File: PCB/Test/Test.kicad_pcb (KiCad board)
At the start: 2 copper layers, 50 x 50 mm, 16 parts, among them J1 USB-C, J2 USB-C, J3 USB-C, J4 USB-C, J5 USB-C, J6 USB-C, J7 USB-C, J8 USB-C, U1 ESP32-PICO-MINI-02, U2 ESP32-PICO-MINI-02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

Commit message: rotate direction
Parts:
- added J9: Conn_01x04, RevK:JLC-PinHeader_1x04_P2.54mm_Right, F.Cu at (104.0, 98.0)
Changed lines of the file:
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@@
   (net 327 "unconnected-(J8-PadB8)")
   (net 328 "unconnected-(J8-PadS1)")
+  (net 329 "unconnected-(J9-Pad1)")
+  (net 330 "unconnected-(J9-Pad2)")
+  (net 331 "unconnected-(J9-Pad3)")
+  (net 332 "unconnected-(J9-Pad4)")
   (footprint "RevK:ESP32-PICO-MINI-02" (layer "F.Cu")
     (at 65 75 90)
@@
     )
   )
+  (footprint "RevK:JLC-PinHeader_1x04_P2.54mm_Right" (layer "F.Cu")
+    (at 104 98)
+    (descr "Through hole angled pin header, 1x04, 2.54mm pitch, 6mm pin length, single row")
+    (tags "Through hole angled pin header THT 1x04 2.54mm single row")
+    (property "Sheetfile" "Test.kicad_sch")
+    (property "Sheetname" "")
+    (attr through_hole)
+    (fp_text reference "J9" (at 4.385 -2.27) (layer "F.SilkS") hide
+      (effects (font (size 1 1) (thickness 0.15)))
+    )
+    (fp_text value "Conn_01x04" (at -6.08 0.655 270) (layer "F.Fab") hide
+      (effects (font (size 1 1) (thickness 0.15)))
+    )
+    (fp_text user "${REFERENCE}" (at 0 2.77) (layer "F.Fab")
+      (effects (font (size 1 1) (thickness 0.15)))
+    )
+    (fp_line (start -5.08 1.27) (end -5.08 -1.27) (layer "F.CrtYd") (width 0.12))
+    (fp_line (start -5.08 -1.27) (end 5.08 -1.27) (layer "F.CrtYd") (width 0.12))
+    (fp_line (start 5.08 1.27) (end -5.08 1.27) (layer "F.CrtYd") (width 0.12))
+    (fp_line (start 5.08 -1.27) (end 5.08 1.27) (layer "F.CrtYd") (width 0.12))
+    (fp_line (start 0.95 -0.32) (end 0.95 1.5) (layer "F.Fab") (width 0.1))
+    (fp_line (start 4.445 1.5) (end 5.08 2.135) (layer "F.Fab") (width 0.1))
+    (fp_line (start -3.49 -0.32) (end -4.13 -0.32) (layer "F.Fab") (width 0.1))
+    (fp_line (start -4.13 4.04) (end -4.13 10.04) (layer "F.Fab") (width 0.1))
+    (fp_line (start -0.95 4.04) (end -0.95 10.04) (layer "F.Fab") (width 0.1))
+    (fp_line (start 5.08 4.04) (end -5.08 4.04) (layer "F.Fab") (width 0.1))
+    (fp_line (start -0.95 -0.32) (end -0.95 1.5) (layer "F.Fab") (width 0.1))
+    (fp_line (start 3.49 4.04) (end 3.49 10.04) (layer "F.Fab") (width 0.1))
+    (fp_line (start 0.95 4.04) (end 0.95 10.04) (layer "F.Fab") (width 0.1))
+    (fp_line (start -0.95 10.04) (end -1.59 10.04) (layer "F.Fab") (width 0.1))
+    (fp_line (start 1.59 -0.32) (end 0.95 -0.32) (layer "F.Fab") (width 0.1))
+    (fp_line (start -3.49 4.04) (end -3.49 10.04) (layer "F.Fab") (width 0.1))
+    (fp_line (start -3.49 -0.32) (end -3.49 1.5) (layer "F.Fab") (width 0.1))
+    (fp_line (start -1.59 -0.32) (end -1.59 1.5) (layer "F.Fab") (width 0.1))
+    (fp_line (start -5.08 4.04) (end -5.08 1.5) (layer "F.Fab") (width 0.1))
+    (fp_line (start 1.59 10.04) (end 0.95 10.04) (layer "F.Fab") (width 0.1))
+    (fp_line (start 4.13 4.04) (end 4.13 10.04) (layer "F.Fab") (width 0.1))
+    (fp_line (start 5.08 2.135) (end 5.08 4.04) (layer "F.Fab") (width 0.1))
+    (fp_line (start 1.59 4.04) (end 1.59 10.04) (layer "F.Fab") (width 0.1))
+    (fp_line (start 4.13 -0.32) (end 3.49 -0.32) (layer "F.Fab") (width 0.1))
+    (fp_line (start -1.59 4.04) (end -1.59 10.04) (layer "F.Fab") (width 0.1))
+    (fp_line (start 3.49 -0.32) (end 3.49 1.5) (layer "F.Fab") (width 0.1))
+    (fp_line (start 4.13 10.04) (end 3.49 10.04) (layer "F.Fab") (width 0.1))
+    (fp_line (start -4.13 -0.32) (end -4.13 1.5) (layer "F.Fab") (width 0.1))
+    (fp_line (start 1.59 -0.32) (end 1.59 1.5) (layer "F.Fab") (width 0.1))
+    (fp_line (start 4.13 -0.32) (end 4.13 1.5) (layer "F.Fab") (width 0.1))
+    (fp_line (start -3.49 10.04) (end -4.13 10.04) (layer "F.Fab") (width 0.1))
+    (fp_line (start -5.08 1.5) (end 4.445 1.5) (layer "F.Fab") (width 0.1))
+    (fp_line (start -0.95 -0.32) (end -1.59 -0.32) (layer "F.Fab") (width 0.1))
+    (pad "1" thru_hole rect (at -3.81 0 270) (size 1.7 1.7) (drill 1) (layers *.Cu *.Mask)
+      (net 329 "unconnected-(J9-Pad1)") (pinfunction "Pin_1") (pintype "passive"))
+    (pad "2" thru_hole oval (at -1.27 0 270) (size 1.7 1.7) (drill 1) (layers *.Cu *.Mask)
+      (net 330 "unconnected-(J9-Pad2)") (pinfunction "Pin_2") (pintype "passive"))
+    (pad "3" thru_hole oval (at 1.27 0 270) (size 1.7 1.7) (drill 1) (layers *.Cu *.Mask)
+      (net 331 "unconnected-(J9-Pad3)") (pinfunction "Pin_3") (pintype "passive"))
+    (pad "4" thru_hole circle (at 3.81 0 270) (size 1.7 1.7) (drill 1) (layers *.Cu *.Mask)
+      (net 332 "unconnected-(J9-Pad4)") (pinfunction "Pin_4") (pintype "passive"))
+    (model "${KICAD6_3DMODEL_DIR}/Connector_PinHeader_2.54mm.3dshapes/PinHeader_1x04_P2.54mm_Horizontal.wrl"
+      (offset (xyz 3.81 0 0))
+      (scale (xyz 1 1 1))
+      (rotate (xyz 0 0 90))
+    )
+  )

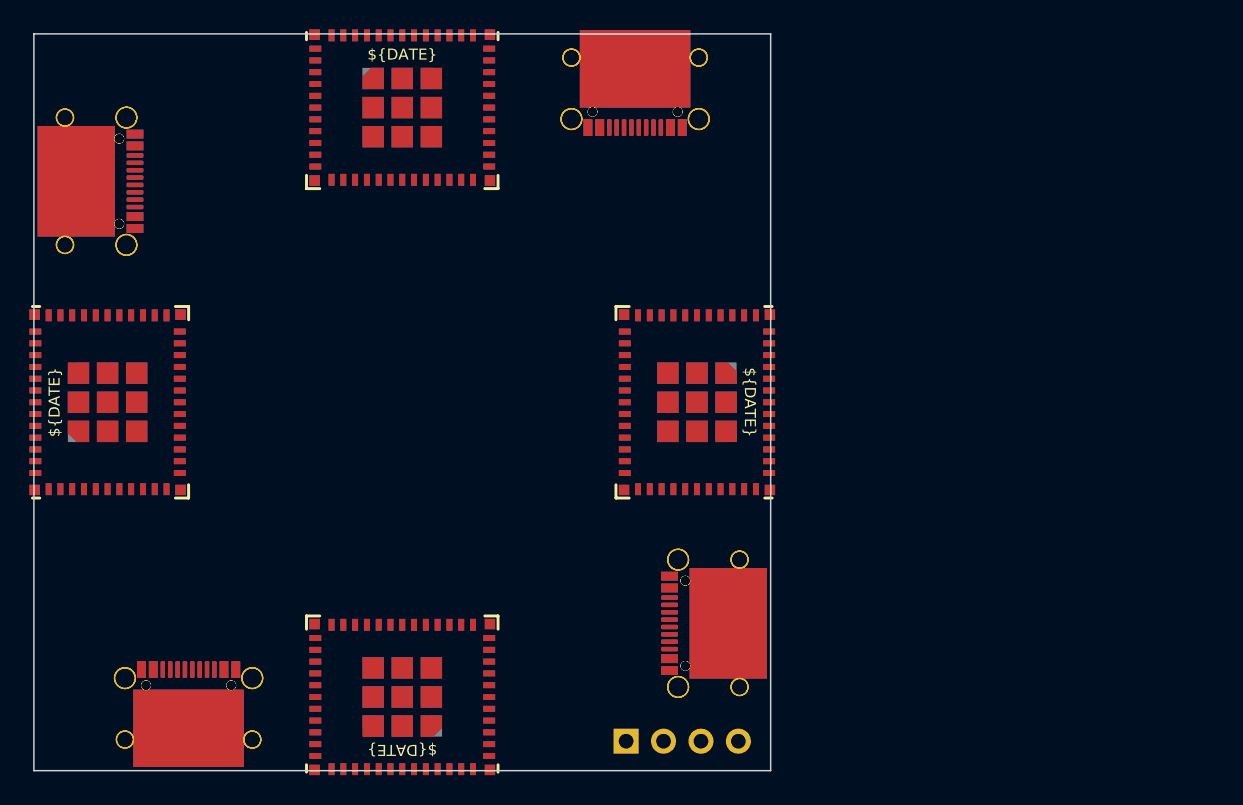
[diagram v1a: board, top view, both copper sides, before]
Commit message: Updated test case
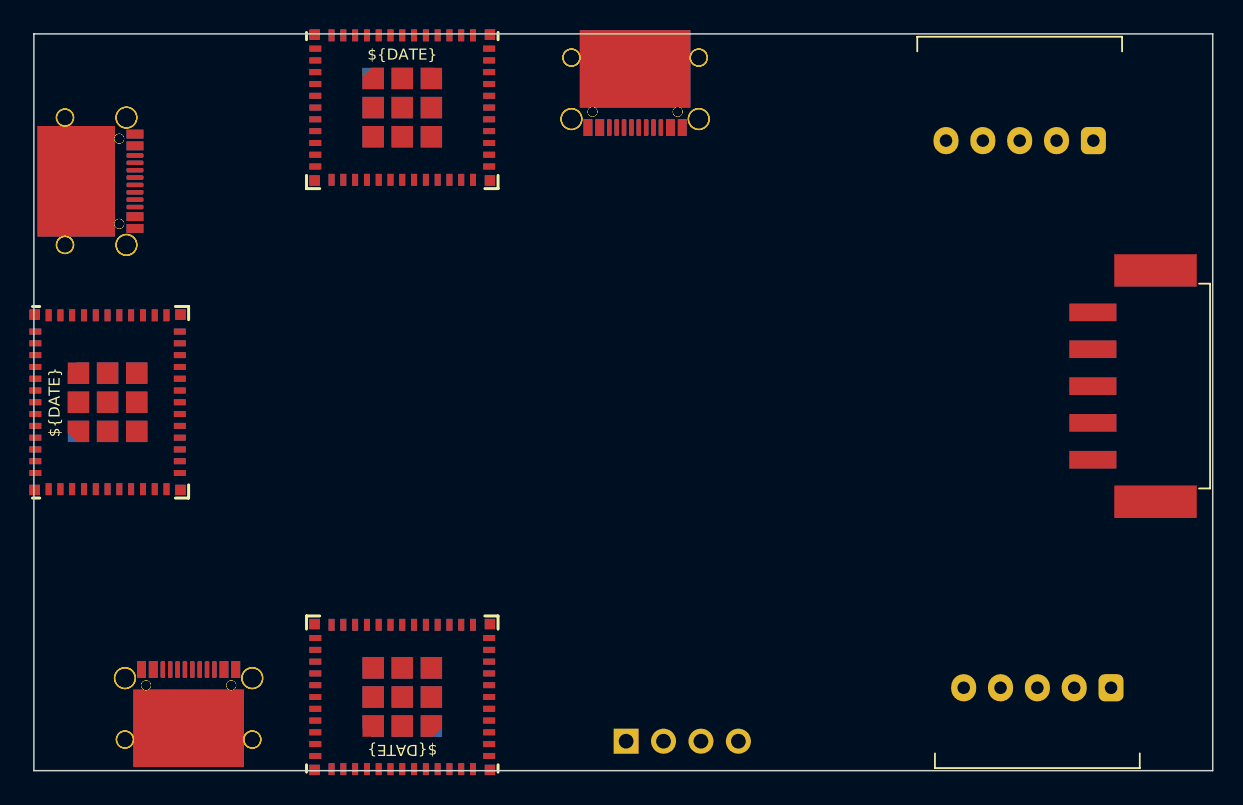
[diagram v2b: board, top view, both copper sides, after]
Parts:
- removed J2, J3: USB-C, RevK:USC16-TR-Round
- removed U1, U8: ESP32-PICO-MINI-02, RevK:ESP32-PICO-MINI-02
- added J10: Conn_01x05, RevK:PTSM-HH-5-RA-P, F.Cu at (128.1, 94.4)
- added J11: Conn_01x05, RevK:PTSM-HH-5-RA, F.Cu at (126.9, 57.2)
- added J12: Conn_01x05, RevK:PTSM-HH-5-RA-P-SMD, F.Cu at (131.9, 73.9)
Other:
- board size 50 x 50 mm -> 80 x 50 mm
